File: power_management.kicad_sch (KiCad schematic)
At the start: 13 parts

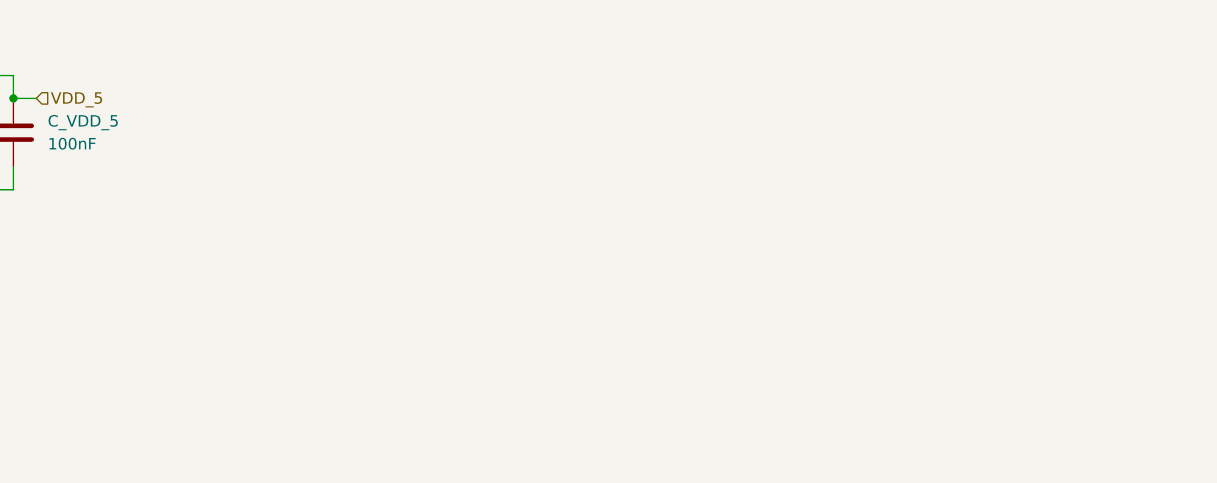
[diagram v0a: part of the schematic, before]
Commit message: :sparkles: Add 12V buck converter
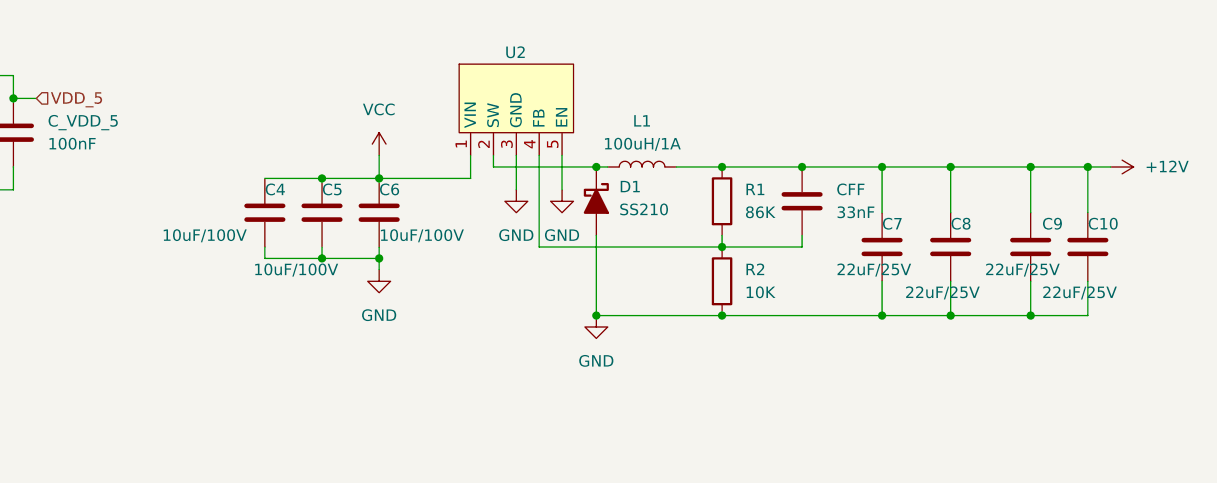
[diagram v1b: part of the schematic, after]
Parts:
- added C10, C7, C8, C9: 22uF/25V, symbol Device:C
- added C4, C5, C6: 10uF/100V, symbol Device:C
- added CFF: 33nF, symbol Device:C
- added D1: SS210, Diode_SMD_AKL:D_SMB, symbol PCM_Diode_Schottky_AKL:SS210
- added L1: 100uH/1A, symbol Device:L
- added R1: 86K, symbol Device:R
- added R2: 10K, symbol Device:R
- added U2: ~, PCM_Package_TO_SOT_SMD_AKL:TO-252-5_TabPin3, symbol CycleIQ:XL7015E1
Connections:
- net GND: now also C10.2, C4.2, C5.2, C6.2, C7.2, C8.2, C9.2, D1.2 (A), R2.2, U2.3 (GND), U2.5 (EN)
- new net: CFF.2, R1.2, R2.1, U2.4 (FB)
- new net: D1.1 (K), L1.1, U2.2 (SW)
- new net +12V: C10.1, C7.1, C8.1, C9.1, CFF.1, L1.2, R1.1
- new net VCC: C4.1, C5.1, C6.1, U2.1 (VIN)

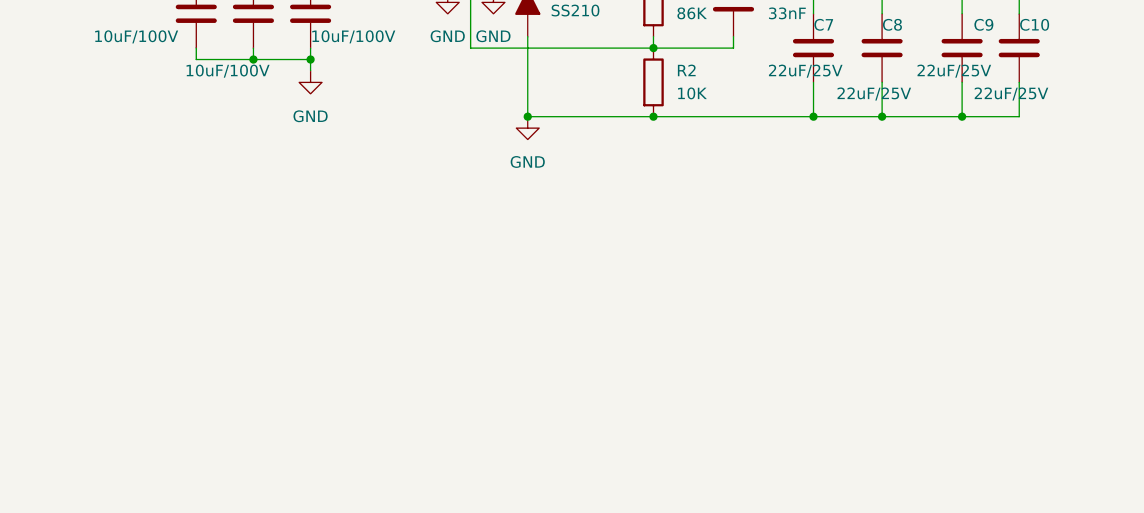
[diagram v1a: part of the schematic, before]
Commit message: :sparkles: Add 5V buck converter
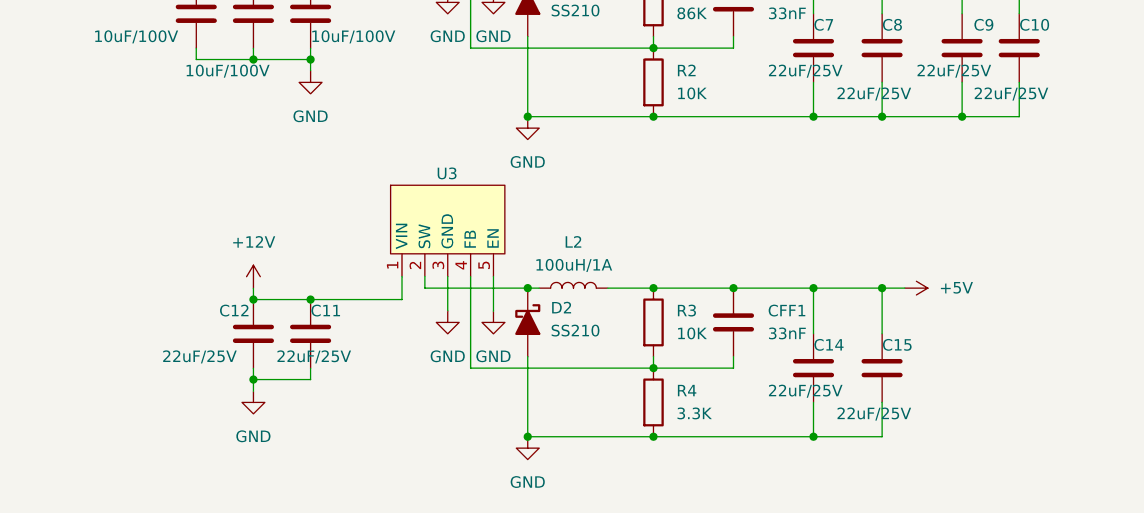
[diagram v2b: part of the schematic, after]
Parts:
- added C11, C12, C14, C15: 22uF/25V, symbol Device:C
- added CFF1: 33nF, symbol Device:C
- added D2: SS210, Diode_SMD_AKL:D_SMB, symbol PCM_Diode_Schottky_AKL:SS210
- added L2: 100uH/1A, symbol Device:L
- added R3: 10K, symbol Device:R
- added R4: 3.3K, symbol Device:R
- added U3: ~, PCM_Package_TO_SOT_SMD_AKL:TO-252-5_TabPin3, symbol CycleIQ:XL7015E1
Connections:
- net +12V: now also C11.1, C12.1, U3.1 (VIN)
- net GND: now also C11.2, C12.2, C14.2, C15.2, D2.2 (A), R4.2, U3.3 (GND), U3.5 (EN)
- new net: CFF1.2, R3.2, R4.1, U3.4 (FB)
- new net: D2.1 (K), L2.1, U3.2 (SW)
- new net +5V: C14.1, C15.1, CFF1.1, L2.2, R3.1

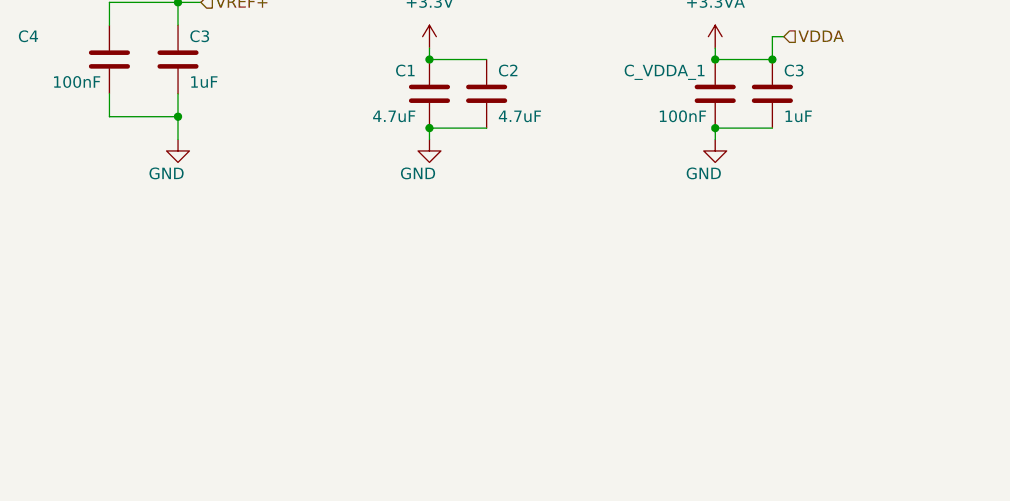
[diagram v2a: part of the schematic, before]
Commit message: :sparkles: Add 3.3V linear regulators
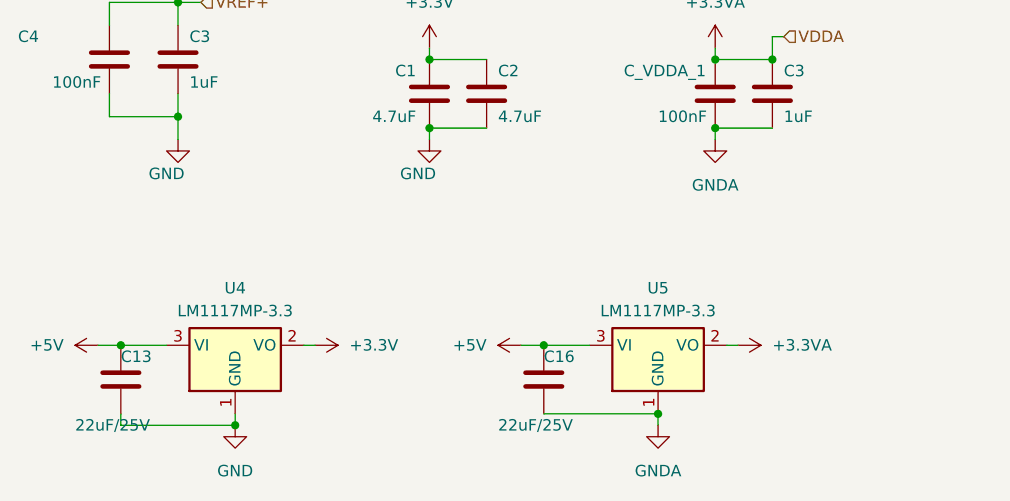
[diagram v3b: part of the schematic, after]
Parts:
- added C13, C16: 22uF/25V, symbol Device:C
- added U4, U5: LM1117MP-3.3, Package_TO_SOT_SMD:SOT-223-3_TabPin2, symbol Regulator_Linear:LM1117MP-3.3
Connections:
- net +3.3V: now also U4.2 (VO)
- net +3.3VA: now also U5.2 (VO)
- net +5V: now also C13.1, C16.1, U4.3 (VI), U5.3 (VI)
- net GND: now also C13.2, U4.1 (GND); no longer C3.2, C_VDDA_1.2
- new net GNDA: C16.2, C3.2, C_VDDA_1.2, U5.1 (GND)

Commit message: 📂 Commit before drastic power board changes
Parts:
- added C25, C26, C27, C28: 680uF, Capacitor_THT:C_Radial_D16.0mm_H25.0mm_P7.50mm, symbol Device:C
- added C_VDD_10, C_VDD_11, C_VDD_12, C_VDD_13, C_VDD_6, C_VDD_7, C_VDD_8, C_VDD_9: 100nF, PCM_Capacitor_SMD_AKL:C_0201_0603Metric, symbol Device:C
- C1, C2, C3: footprint (none) -> PCM_Capacitor_SMD_AKL:C_0603_1608Metric
- C10: renamed from C11; footprint (none) -> PCM_Capacitor_SMD_AKL:C_1206_3216Metric
- C11: renamed from C7; footprint (none) -> PCM_Capacitor_SMD_AKL:C_1206_3216Metric
- C12: renamed from C14; footprint (none) -> PCM_Capacitor_SMD_AKL:C_1206_3216Metric
- C13: renamed from C8; footprint (none) -> PCM_Capacitor_SMD_AKL:C_1206_3216Metric
- C14: renamed from C15; footprint (none) -> PCM_Capacitor_SMD_AKL:C_1206_3216Metric
- C15: renamed from C9; footprint (none) -> PCM_Capacitor_SMD_AKL:C_1206_3216Metric
- C16: renamed from C10; footprint (none) -> PCM_Capacitor_SMD_AKL:C_1206_3216Metric
- C2: renamed from C13; footprint (none) -> PCM_Capacitor_SMD_AKL:C_1206_3216Metric
- C3: renamed from C1; footprint (none) -> PCM_Capacitor_SMD_AKL:C_1206_3216Metric
- C4, C_VDDA_1, C_VDD_1, C_VDD_2, C_VDD_3, C_VDD_4, C_VDD_5: footprint (none) -> PCM_Capacitor_SMD_AKL:C_0201_0603Metric
- C4: renamed from C2; footprint (none) -> PCM_Capacitor_SMD_AKL:C_1206_3216Metric
- C5: renamed from C16; footprint (none) -> PCM_Capacitor_SMD_AKL:C_1206_3216Metric
- C6: renamed from C4; footprint (none) -> PCM_Capacitor_SMD_AKL:C_1210_3225Metric
- C7: renamed from C5; footprint (none) -> PCM_Capacitor_SMD_AKL:C_1210_3225Metric
- C8: renamed from C12; footprint (none) -> PCM_Capacitor_SMD_AKL:C_1206_3216Metric
- C9: renamed from C6; footprint (none) -> PCM_Capacitor_SMD_AKL:C_1210_3225Metric
- renumbered CFF to CFF1, CFF1 to CFF2, U4 to U2, U5 to U3, U2 to U4, U3 to U5
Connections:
- net VCAP_2 is gone; now on net VCAP: C1.1
- net +3.3V: now also C_VDD_10.1, C_VDD_11.1, C_VDD_12.1, C_VDD_13.1, C_VDD_6.1, C_VDD_7.1, C_VDD_8.1, C_VDD_9.1
- net GND: now also C25.2, C26.2, C27.2, C28.2, C_VDD_10.2, C_VDD_11.2, C_VDD_12.2, C_VDD_13.2, C_VDD_6.2, C_VDD_7.2, C_VDD_8.2, C_VDD_9.2
- net VCC: now also C25.1, C26.1, C27.1, C28.1
- net VCAP_1 renamed VCAP
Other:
- moved on the sheet: C_VDD_1, C_VDD_2, C_VDD_3, C_VDD_4, C_VDD_5
